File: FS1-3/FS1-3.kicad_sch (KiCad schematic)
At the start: 63 parts, among them U1 74LS54, U10 74LS51, U11 74HC02, U12 74AHC04, U13 74LS51, U14 74HC00, U15 74LS51, U16 74LS51, U17 74LS51, U18 74AHC04, U19 74LS51, U2 74LS51, U20 74LS51, U21 74LS51, U22 74AHC04, U23 74LS51, U24 74LS51, U25 74LS51, U26 74LS51, U27 74LS51, U28 74LS51, U29 74LS51, U3 74LS54, U30 74AHC04, U31 74LS51, U32 74LS54, U33 74LS54, U34 74LS54, U35 74LS54, U36 74LS51, U37 74LS51, U38 74LS51, U39 74LS51, U4 74LS51, U40 74AHC04, U41 74AHC04, U42 74HC02, U43 74HC00, U44 74LS51, U45 74LS51, U46 74LS51, U47 74LS51, U48 74AHC04, U49 74AHC04, U5 74LS54, U50 74AHC04, U51 74LS51, U52 74LS51, U53 74LS51, U54 74LS51, U55 74LS51, U56 74LS51, U57 74LS51, U58 74LS51, U59 74LS51, U6 74LS51, U60 74LS51, U61 74LS51, U62 74LS51, U7 74LS54, U8 74LS51, U9 74AHC04

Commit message: initial work on schematics for a backplane to which all boards will be attached.
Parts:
- renumbered U36 to 1A_P2, U32 to 1B_P2
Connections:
- net +NAND: now also U16.9, U21.9, U26.9, U31.9, U59.9, U60.9, U61.9, U62.9; no longer U16.4, U21.4, U26.4, U31.4, U59.4, U60.4, U61.4, U62.4
- net +P10: now also U37.1; no longer U37.2
- net +P11: now also 1A_P2.1; no longer 1A_P2.2
- net +P4: now also U2.1; no longer U2.2
- net +P5: now also U4.1; no longer U4.2
- net +P6: now also U6.1; no longer U6.2
- net +P7: now also U8.1; no longer U8.2
- net +P8: now also U39.1; no longer U39.2
- net +P9: now also U38.1; no longer U38.2
- net +RD0: now also U2.9; no longer U2.4
- net +RD1: now also U4.9; no longer U4.4
- net +RD2: now also U6.9; no longer U6.4
- net +RD3: now also U8.9; no longer U8.4
- net +RD4: now also U39.9; no longer U39.4
- net +RD5: now also U38.9; no longer U38.4
- net +RD6: now also U37.9; no longer U37.4
- net +RD7: now also 1A_P2.9; no longer 1A_P2.4
- net +SOXOR: now also U16.13, U21.13, U26.13, U31.13, U59.13, U60.13, U61.13, U62.13; no longer U16.3, U21.3, U26.3, U31.3, U59.3, U60.3, U61.3, U62.3
- net +VUR: now also U12.1, U28.9, U29.9, U41.1, U51.9, U52.9; no longer U12.3, U28.4, U29.4, U41.3, U51.4, U52.4
- net +Z0: now also U16.8; no longer U16.6
- net +Z1: now also U21.8; no longer U21.6
- net +Z2: now also U26.8; no longer U26.6
- net +Z3: now also U31.8; no longer U31.6
- net +Z4: now also U62.8; no longer U62.6
- net +Z5: now also U61.8; no longer U61.6
- net +Z6: now also U60.8; no longer U60.6
- net +Z7: now also U59.8; no longer U59.6
- net -C1: now also U12.1, U13.11, U15.1, U20.8; no longer U12.11, U13.5, U15.2, U20.6
- net -C5: now also U41.1, U55.8, U56.11, U58.1; no longer U41.11, U55.6, U56.5, U58.2
- net -X1: now also U11.2, U14.1, U17.9, U9.1; no longer U11.5, U14.4, U17.4, U9.5
- net -X2: now also U23.9, U25.9, U9.1; no longer U23.4, U25.4, U9.13
- net -X3: now also U11.2, U12.1, U14.1, U27.9; no longer U11.11, U12.13, U14.12, U27.4
- net -X4: now also U40.1, U42.2, U45.9, U58.9; no longer U40.11, U42.8, U45.4, U58.4
- net -X5: now also U40.1, U42.2, U43.1, U44.9; no longer U40.5, U42.5, U43.4, U44.4
- net -X6: now also U40.1, U47.9, U57.9; no longer U40.13, U47.4, U57.4
- net -X7: now also U41.1, U42.2, U43.1, U46.9; no longer U41.13, U42.11, U43.12, U46.4
- net -XOR: now also U14.1, U20.13, U28.13, U43.1, U52.13, U55.13; no longer U14.9, U20.3, U28.3, U43.9, U52.3, U55.3
- net -Y1: now also U11.3, U14.2, U17.11, U4.8, U9.1; no longer U11.6, U14.5, U17.5, U4.6, U9.3
- net -Y2: now also U23.11, U25.11, U6.8; no longer U23.5, U25.5, U6.6
- net -Y3: now also U11.3, U14.2, U27.11, U8.8; no longer U11.12, U14.13, U27.5, U8.6
- net -Y4: now also U39.8, U40.1, U42.3, U45.11, U58.11; no longer U39.6, U40.9, U42.9, U45.5, U58.5
- net -Y5: now also U38.8, U40.1, U42.3, U43.2, U44.11; no longer U38.6, U40.3, U42.6, U43.5, U44.5
- net -Y6: now also U37.8, U47.11, U57.11; no longer U37.6, U47.5, U57.5
- net -Y7: now also 1A_P2.8, U42.3, U43.2, U46.11; no longer 1A_P2.6, U42.12, U43.13, U46.5
- net AC/X: now also 1A_P2.10, U2.11, U37.11, U38.11, U39.11, U4.11, U6.11, U8.11; no longer 1A_P2.5, U2.5, U37.5, U38.5, U39.5, U4.5, U6.5, U8.5
- net C0: now also U15.8; no longer U15.6
- net C4: now also U58.8; no longer U58.6
- net P/Y: now also 1A_P2.13, U2.13, U37.13, U38.13, U39.13, U4.13, U6.13, U8.13; no longer 1A_P2.3, U2.3, U37.3, U38.3, U39.3, U4.3, U6.3, U8.3
- net X0: now also U10.9, U11.2, U15.9, U9.1; no longer U10.4, U11.8, U15.4, U9.11
- net Y0: now also U10.11, U11.3, U15.11, U2.8, U9.1; no longer U10.5, U11.9, U15.5, U2.6, U9.9
- net at U12.2: now also U27.1; no longer U27.2
- net at U43.3: now also U58.13; no longer U58.3
- net at U41.2: now also U46.1; no longer U46.2
- net at U14.3: now also U15.13; no longer U15.3
- net at U9.2: now also U23.1; no longer U23.2
- net at U40.2: now also U47.1; no longer U47.2
- new net: U41.1, U45.8, U56.9
- new net: U41.2, U56.1
- new net: U14.3, U28.11
- new net: U12.2, U27.13
- new net: U27.8, U29.1, U30.1
- new net: U40.2, U44.1
- new net: U40.2, U44.13
- new net: U44.8, U49.1, U54.1
- new net: U43.3, U52.11
- new net: U11.1, U20.1, U21.11
- new net: U14.3, U20.11
- new net: U18.1, U19.9, U20.9, U25.8
- new net: U11.1, U14.2, U16.11
- new net: U42.1, U43.2, U60.11
- new net: U43.3, U57.13
- new net: U17.8, U18.1, U19.1
- new net: U18.2, U19.11
- new net: U40.2, U45.1
- new net: U42.1, U52.1, U59.11
- new net: U48.1, U52.8, U53.11, U57.1
- new net: U54.8, U61.1
- new net: U42.1, U55.1, U61.11
- new net: U56.8, U62.1
- new net: U42.1, U43.2, U62.11
- new net: U41.2, U51.13
- new net: U49.1, U54.9, U55.9, U57.8
- new net: U17.13, U9.2
- new net: U11.1, U28.1, U31.11
- new net: U22.1, U24.11, U25.1, U28.8
- new net: U46.8, U50.1, U51.1
- new net: U50.2, U51.11
- new net: U43.3, U55.11
- new net: U13.8, U16.1
- new net: U22.2, U24.13
- new net: U49.2, U54.11
- new net: U49.2, U54.13
- new net: U14.3, U25.13
- new net: U19.8, U21.1
- new net: U53.8, U60.1
- new net: U41.2, U46.13
- new net: U40.2, U47.13
- new net: U29.11, U30.2
- new net: U12.2, U29.13
- new net: U29.8, U31.1
- new net: U48.2, U53.13
- new net: U40.2, U45.13
- new net: U18.2, U19.13
- new net: U11.1, U14.2, U26.11
- new net: U10.1, U9.2
- new net: U10.13, U9.2
- new net: U10.8, U12.1, U13.9
- new net: U47.8, U48.1, U53.9
- new net: U48.2, U53.1
- new net: U12.2, U13.1
- new net: U12.2, U13.13
- new net: U51.8, U59.1
- new net: U41.2, U56.13
- new net: U23.13, U9.2
- new net: U22.1, U23.8, U24.9
- new net: U22.2, U24.1
- new net: U24.8, U26.1
- new net: U17.1, U9.2
- no-connect marks 0 -> 2

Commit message: first review and many fixes to FS1-3 board
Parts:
- removed U1, U3, U5, U7: 74LS54, symbol 74xx:74LS54
- removed U10, U13, U15, U16, U17, U19, U2, U20, U21, U23, U24, U25, U26, U27, U28, U29, U31, U4, U6, U8: 74LS51, symbol 74xx:74LS51
- removed U11 (x4): 74HC02, symbol 74xx:74HC02
- removed U12 (x5), U18 (x2), U22 (x2), U30, U9 (x6): 74AHC04, symbol 74xx:74AHC04
- removed U14 (x4): 74HC00, symbol 74xx:74HC00
- gave numbers to parts that had none: 1
- renumbered U37 to 1A_P2A_, 1A_P2 to 1A_P2A_, 1B_P2 to 1B_P2A_, U40 to 1C_P2A_, U41 to 1C_P2A_, U48 to 1C_P2A_, U46 to 1D_P2A_, U47 to 1D_P2A_, U52 to 1E_P2A_, U51 to 1E_P2A_, U60 to 1F_P2A_, U59 to 1F_P2A_, U42 to 2C_P2A_, U39 to 3A_P2A_, U38 to 3A_P2A_, U33 to 3B_P2A_, U42 to 3C_P2A_, U57 to 3D_P2A_, U53 to 3D_P2A_, U49 to 3E_P2A_, U48 to 3E_P2A_, U41 to 3E_P2A_, U61 to 3F_P2A_, U62 to 3F_P2A_, U43 to 4C_P2A_, U34 to 5A_P2A_, U35 to 5B_P2A_, U41 to 5C_P2A_, U40 to 5C_P2A_, U44 to 5D_P2A_, U45 to 5D_P2A_, U55 to 5E_P2A_, U54 to 5E_P2A_, U58 to 5F_P2A_, U56 to 5F_P2A_
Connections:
- net +AC4: now also CONECTOR_P2A.62 (P62)
- net +AC5: now also 5A_P2A_.13, CONECTOR_P2A.66 (P66); no longer 5A_P2A_.1
- net +AC6: now also CONECTOR_P2A.15 (P15)
- net +AC7: now also CONECTOR_P2A.38 (P38)
- net +CI10: now also 3B_P2A_.5, CONECTOR_P2A.16 (P16); no longer 3B_P2A_.4
- net +CI11: now also 1B_P2A_.5, CONECTOR_P2A.39 (P39); no longer 1B_P2A_.4
- net +CI8: now also CONECTOR_P2A.63 (P63)
- net +CI9: now also 5A_P2A_.5, CONECTOR_P2A.64 (P64); no longer 5A_P2A_.4
- net +NAND: now also 1F_P2A_.1, 1F_P2A_.2, 3F_P2A_.4, CONECTOR_P2A.60 (P60); no longer 1F_P2A_.9, 1F_P2A_.9, 3F_P2A_.9
- net +P10: now also 1A_P2A_.2, CONECTOR_P2A.40 (P40); no longer 1A_P2A_.1
- net +P11: now also CONECTOR_P2A.4 (P4)
- net +P8: now also CONECTOR_P2A.52 (P52)
- net +P9: now also 3A_P2A_.3, CONECTOR_P2A.17 (P17); no longer 3A_P2A_.1
- net +RD4: now also CONECTOR_P2A.55 (P55)
- net +RD5: now also 3A_P2A_.4, CONECTOR_P2A.53 (P53); no longer 3A_P2A_.9
- net +RD6: now also 1A_P2A_.4, CONECTOR_P2A.41 (P41); no longer 1A_P2A_.9
- net +RD7: now also CONECTOR_P2A.42 (P42)
- net +RE10: now also CONECTOR_P2A.20 (P20)
- net +RE11: now also CONECTOR_P2A.43 (P43)
- net +RE8: now also 5B_P2A_.10, CONECTOR_P2A.67 (P67); no longer 5B_P2A_.9
- net +RE9: now also CONECTOR_P2A.31 (P31)
- net +SOXOR: now also 1F_P2A_.10, 1F_P2A_.4, 3F_P2A_.1, 3F_P2A_.2, CONECTOR_P2A.34 (P34); no longer 1F_P2A_.13, 1F_P2A_.13, 3F_P2A_.13, 3F_P2A_.13
- net +VUR: now also 1E_P2A_.1, 1E_P2A_.4, CONECTOR_P2A.2 (P2), U41.3; no longer 1E_P2A_.9, 1E_P2A_.9, U41.1
- net +Z4: now also 3F_P2A_.6, CONECTOR_P2A.56 (P56); no longer 3F_P2A_.8
- net +Z5: now also CONECTOR_P2A.58 (P58)
- net +Z6: now also CONECTOR_P2A.47 (P47)
- net +Z7: now also 1F_P2A_.6, CONECTOR_P2A.37 (P37); no longer 1F_P2A_.8
- net -AC4: now also 5B_P2A_.3, CONECTOR_P2A.28 (P28); no longer 5B_P2A_.2
- net -AC5: now also 5A_P2A_.3, CONECTOR_P2A.30 (P30); no longer 5A_P2A_.2
- net -AC6: now also 3B_P2A_.3, CONECTOR_P2A.51 (P51); no longer 3B_P2A_.2
- net -AC7: now also 1B_P2A_.3, CONECTOR_P2A.3 (P3); no longer 1B_P2A_.2
- net -AC/X: now also 1B_P2A_.2, 3B_P2A_.2, 5A_P2A_.2, 5B_P2A_.2, CONECTOR_P2A.65 (P65); no longer 1B_P2A_.3, 3B_P2A_.3, 5A_P2A_.3, 5B_P2A_.3
- net -C5: now also 3E_P2A_.9, 5F_P2A_.4, 5F_P2A_.9, CONECTOR_P2A.68 (P68); no longer 3E_P2A_.1, 5F_P2A_.1, 5F_P2A_.11
- net -X4: now also 3C_P2A_.9, 5C_P2A_.11, 5D_P2A_.1, 5F_P2A_.3; no longer 3C_P2A_.2, 5C_P2A_.1, 5D_P2A_.9, 5F_P2A_.9
- net -X5: now also 3C_P2A_.5, 4C_P2A_.4, 5C_P2A_.5, 5D_P2A_.4; no longer 3C_P2A_.2, 4C_P2A_.1, 5C_P2A_.1, 5D_P2A_.9
- net -X6: now also 1C_P2A_.13, 1D_P2A_.4, 2C_P2A_.12, 3D_P2A_.10; no longer 1C_P2A_.1, 1D_P2A_.9, 2C_P2A_.2, 3D_P2A_.9
- net -X7: now also 1D_P2A_.13; no longer 1D_P2A_.9
- net -XOR: now also 1E_P2A_.9, 4C_P2A_.10, 4C_P2A_.12, CONECTOR_P2A.61 (P61); no longer 1E_P2A_.13, 4C_P2A_.1, 4C_P2A_.1
- net -Y4: now also 3C_P2A_.8, 5C_P2A_.9, 5D_P2A_.13, 5F_P2A_.2; no longer 3C_P2A_.3, 5C_P2A_.1, 5D_P2A_.11, 5F_P2A_.11
- net -Y5: now also 3A_P2A_.6, 3C_P2A_.6, 4C_P2A_.5, 5C_P2A_.3, 5D_P2A_.5; no longer 3A_P2A_.8, 3C_P2A_.3, 4C_P2A_.2, 5C_P2A_.1, 5D_P2A_.11
- net -Y6: now also 1A_P2A_.6, 1C_P2A_.5, 1D_P2A_.5, 2C_P2A_.11, 3D_P2A_.9; no longer 1A_P2A_.8, 1C_P2A_.1, 1D_P2A_.11, 2C_P2A_.3, 3D_P2A_.11
- net -Y7: now also 1C_P2A_.3, 1D_P2A_.1; no longer 1C_P2A_.1, 1D_P2A_.11
- net AC/X: now also 5A_P2A_.1, CONECTOR_P2A.33 (P33); no longer 1A_P2A_.10, 1A_P2A_.11, 3A_P2A_.11, 3A_P2A_.11, 5A_P2A_.13
- net C1/X: now also 1B_P2A_.4, 3B_P2A_.4, 5A_P2A_.4; no longer 1B_P2A_.5, 3B_P2A_.5, 5A_P2A_.5
- net C4: now also 5F_P2A_.6; no longer 5F_P2A_.8
- net P/Y: now also 1A_P2A_.3, 3A_P2A_.2, CONECTOR_P2A.5 (P5); no longer 1A_P2A_.13, 3A_P2A_.13
- net RE/X: now also 5B_P2A_.9, CONECTOR_P2A.32 (P32); no longer 5B_P2A_.10
- net at 5F_P2A_.1: now also 5C_P2A_.12; no longer 5C_P2A_.2
- net at 4C_P2A_.3: now also 1E_P2A_.13; no longer 1E_P2A_.11
- net at 3D_P2A_.13: now also 4C_P2A_.11; no longer 4C_P2A_.3
- net at 1E_P2A_.10: now also 1F_P2A_.3, 3C_P2A_.1
- net at 1E_P2A_.8, 3D_P2A_.1: now also 3D_P2A_.4, 3E_P2A_.5; no longer 3D_P2A_.11, 3E_P2A_.1
- net at 3F_P2A_.10: now also 3C_P2A_.4, 5E_P2A_.1
- net RD/Y: now reaches 3A_P2A_.10
- net RD/Y: now also 1A_P2A_.10, 1A_P2A_.5, 3A_P2A_.5, CONECTOR_P2A.7 (P7)
- net at 5F_P2A_.8: now also 3F_P2A_.3; no longer 3F_P2A_.1
- net at 5E_P2A_.10: now also 3D_P2A_.8, 3E_P2A_.11, 5E_P2A_.5
- net at 5E_P2A_.11: no longer 4C_P2A_.3
- net at 1D_P2A_.10: now also 1C_P2A_.2
- net at 5D_P2A_.10: now also 5C_P2A_.8
- net at 5F_P2A_.13: now also 3E_P2A_.8; no longer 3E_P2A_.2
- net at 5F_P2A_.10: now also 5C_P2A_.13, 5D_P2A_.8
- removed net ?: CONECTOR_P2A.1 (P1), CONECTOR_P2A.10 (P10), CONECTOR_P2A.11 (P11), CONECTOR_P2A.12 (P12), CONECTOR_P2A.13 (P13), CONECTOR_P2A.14 (P14), CONECTOR_P2A.15 (P15), CONECTOR_P2A.16 (P16), CONECTOR_P2A.17 (P17), CONECTOR_P2A.18 (P18), CONECTOR_P2A.19 (P19), CONECTOR_P2A.2 (P2), CONECTOR_P2A.20 (P20), CONECTOR_P2A.21 (P21), CONECTOR_P2A.22 (P22), CONECTOR_P2A.23 (P23), CONECTOR_P2A.24 (P24), CONECTOR_P2A.25, CONECTOR_P2A.26 (P26), CONECTOR_P2A.27 (P27), CONECTOR_P2A.28 (P28), CONECTOR_P2A.29 (P29), CONECTOR_P2A.3 (P3), CONECTOR_P2A.30 (P30), CONECTOR_P2A.31 (P31), CONECTOR_P2A.32 (P32), CONECTOR_P2A.33 (P33), CONECTOR_P2A.34 (P34), CONECTOR_P2A.35 (P35), CONECTOR_P2A.36 (P36), CONECTOR_P2A.37 (P37), CONECTOR_P2A.38 (P38), CONECTOR_P2A.39 (P39), CONECTOR_P2A.4 (P4), CONECTOR_P2A.40 (P40), CONECTOR_P2A.41 (P41), CONECTOR_P2A.42 (P42), CONECTOR_P2A.43 (P43), CONECTOR_P2A.44 (P44), CONECTOR_P2A.45 (P45), CONECTOR_P2A.46 (P46), CONECTOR_P2A.47 (P47), CONECTOR_P2A.48 (P48), CONECTOR_P2A.49 (P49), CONECTOR_P2A.5 (P5), CONECTOR_P2A.50 (P50), CONECTOR_P2A.51 (P51), CONECTOR_P2A.52 (P52), CONECTOR_P2A.53 (P53), CONECTOR_P2A.54 (P54), CONECTOR_P2A.55 (P55), CONECTOR_P2A.56 (P56), CONECTOR_P2A.57 (P57), CONECTOR_P2A.58 (P58), CONECTOR_P2A.59 (P59), CONECTOR_P2A.6 (P6), CONECTOR_P2A.60 (P60), CONECTOR_P2A.61 (P61), CONECTOR_P2A.62 (P62), CONECTOR_P2A.63 (P63), CONECTOR_P2A.64 (P64), CONECTOR_P2A.65 (P65), CONECTOR_P2A.66 (P66), CONECTOR_P2A.67 (P67), CONECTOR_P2A.68 (P68), CONECTOR_P2A.69 (P69), CONECTOR_P2A.7 (P7), CONECTOR_P2A.70 (P70), CONECTOR_P2A.8 (P8), CONECTOR_P2A.9 (P9)
- new net: 5C_P2A_.6, 5D_P2A_.2
- new net: 5C_P2A_.4, 5D_P2A_.3
- new net: 3E_P2A_.13, 5D_P2A_.6, 5E_P2A_.2
- new net: 1F_P2A_.13, 2C_P2A_.13, 4C_P2A_.13
- new net: 3F_P2A_.13, 5E_P2A_.6
- new net: 3C_P2A_.10, 3F_P2A_.5, 4C_P2A_.9
- new net: 1E_P2A_.3, U41.4
- new net: 1E_P2A_.5, U50.10
- new net: 1D_P2A_.8, 1E_P2A_.2, U50.11
- new net: 4C_P2A_.6, 5E_P2A_.9
- new net: 3E_P2A_.10, 5E_P2A_.3
- new net: 3E_P2A_.12, 5E_P2A_.4
- new net: 1F_P2A_.9, 3D_P2A_.6
- new net: 4C_P2A_.8, 5F_P2A_.5
- new net: 1C_P2A_.4, 1D_P2A_.9
- new net: 1C_P2A_.12, 1D_P2A_.2
- new net: 3D_P2A_.3, 3E_P2A_.6
- new net: 5C_P2A_.10, 5D_P2A_.9
- new net: 1C_P2A_.8, 3D_P2A_.2
- new net: 1C_P2A_.9, 1D_P2A_.6, 3D_P2A_.5
- new net: 1E_P2A_.6, 1F_P2A_.5
- new net: 1C_P2A_.6, 1D_P2A_.3
- new net +C4: CONECTOR_P2A.57 (P57)
- new net CI/X: CONECTOR_P2A.29 (P29)
- new net GND: CONECTOR_P2A.70 (P70)
- new net VCC: CONECTOR_P2A.1 (P1)
- now unconnected: 1F_P2A_.11, 3F_P2A_.11
- no-connect marks 2 -> 48
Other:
- moved on the sheet: 1C_P2A_A, 1C_P2A_D, 1C_P2A_F, 1D_P2A_A, 1E_P2A_A, 1F_P2A_A, 3A_P2A_A, 3C_P2A_C, 3E_P2A_D, 3E_P2A_F, 4C_P2A_C, 5B_P2A_A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

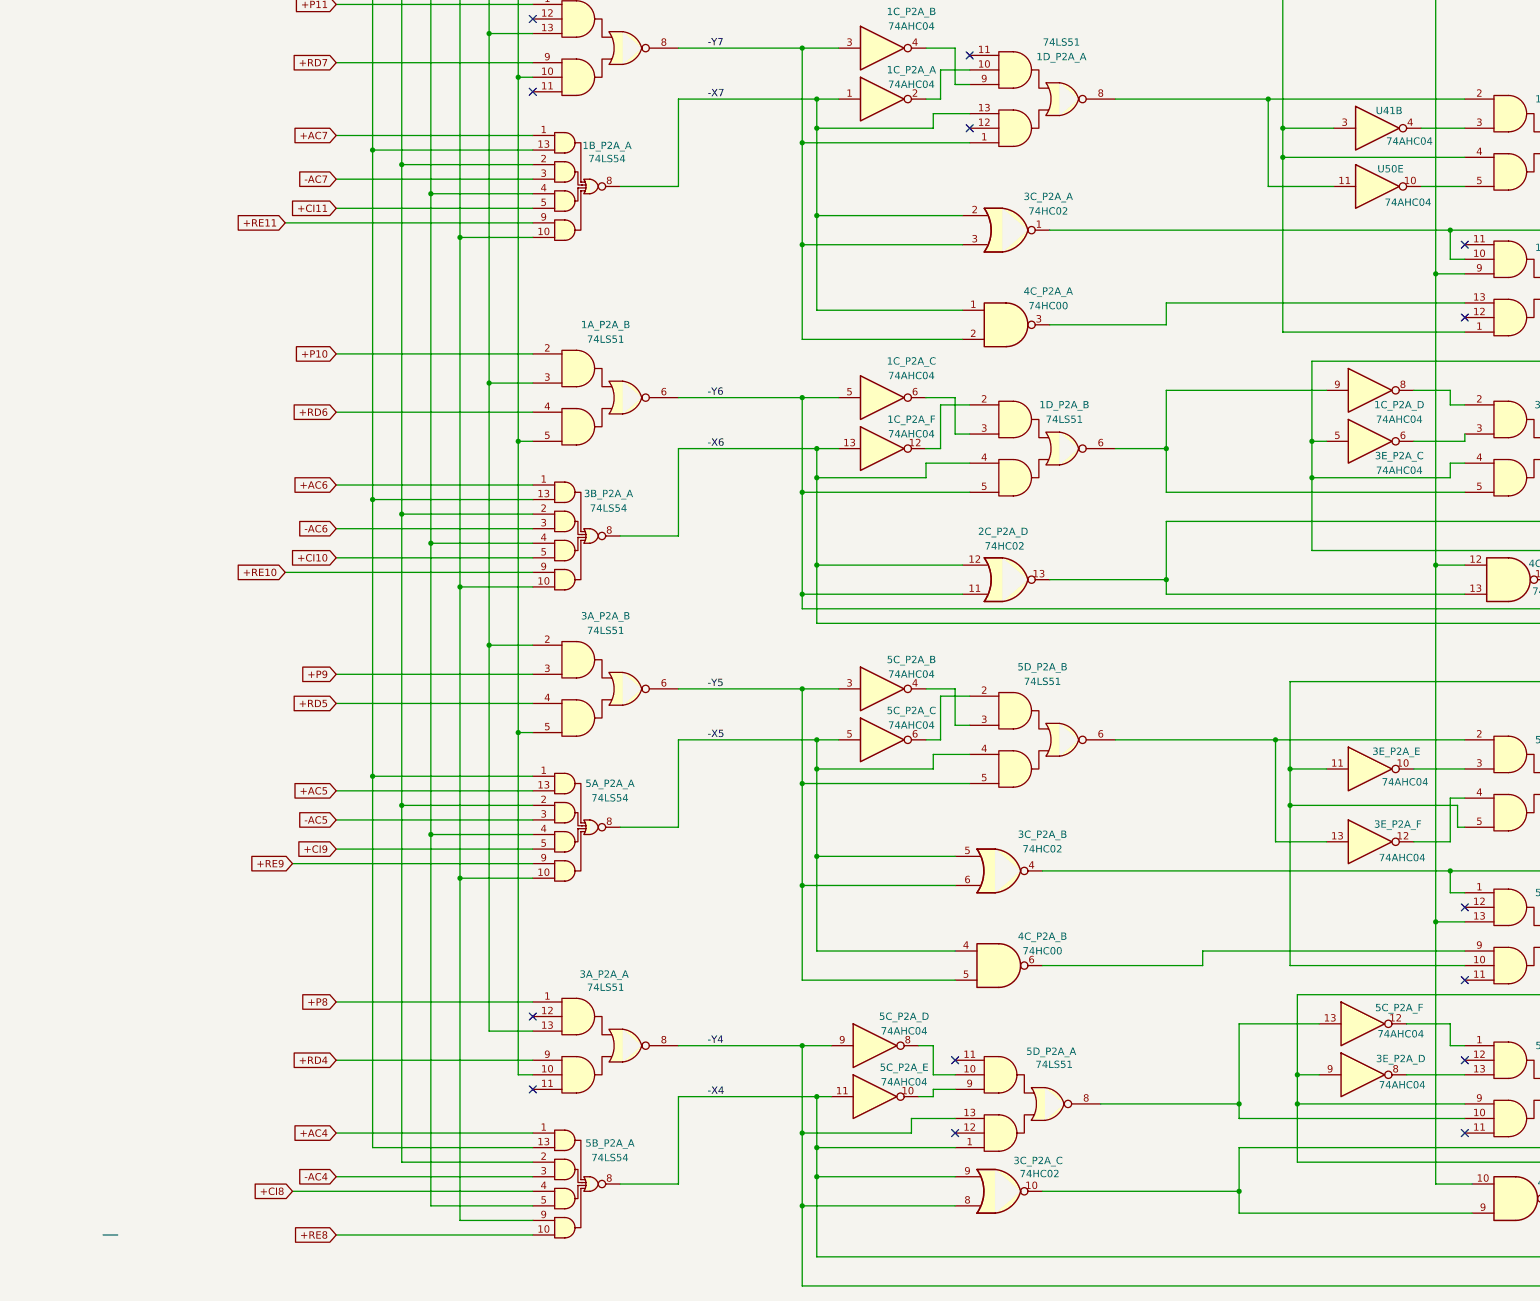
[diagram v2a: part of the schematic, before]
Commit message: adding references to a couple NOT gates that are not annotated in the original schematics.
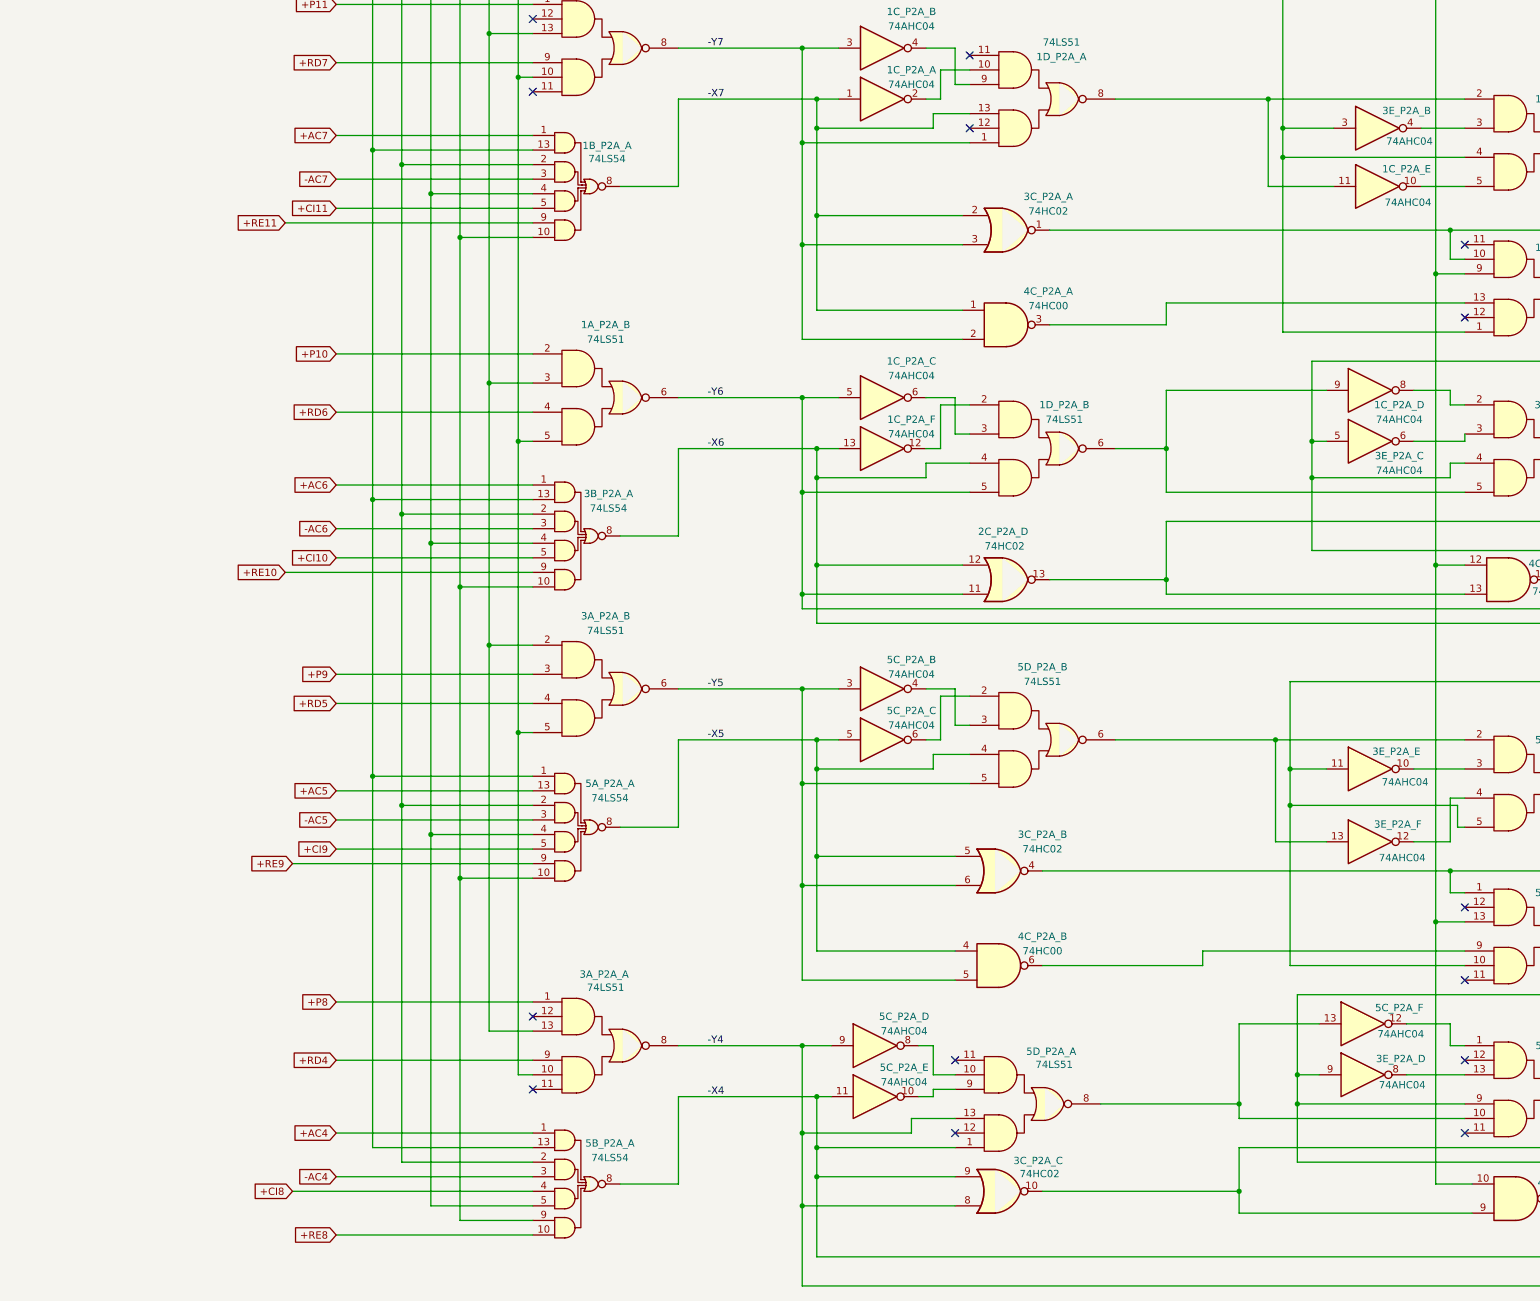
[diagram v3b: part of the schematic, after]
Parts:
- renumbered U50 to 1C_P2A_, U41 to 3E_P2A_
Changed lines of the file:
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@@
 		)
 	)
-	(polyline
-		(pts
-			(xy 219.71 308.61) (xy 217.17 308.61)
-		)
-		(stroke
-			(width 0)
-			(type default)
-		)
-	)
 	(wire
 		(pts
@@
 		(in_pos_files yes)
 		(dnp no)
-		(property "Reference" "U?"
-			(at 441.452 112.522 0)
+		(property "Reference" "3E_P2A_"
+			(at 444.5 112.522 0)
 			(show_name no)
 			(do_not_autoplace no)
@@
 			(project "patinhofeio"
 				(path "/aca06203-542d-4682-a7e3-8839e24cce95/513c6191-fb8d-4702-a239-0db81c50d326"
-					(reference "U?")
+					(reference "3E_P2A_")
 					(unit 2)
 				)
@@
 		(in_pos_files yes)
 		(dnp no)
-		(property "Reference" "U?"
-			(at 441.706 122.682 0)
+		(property "Reference" "1C_P2A_"
+			(at 444.5 122.682 0)
 			(show_name no)
 			(do_not_autoplace no)
@@
 			(project "patinhofeio"
 				(path "/aca06203-542d-4682-a7e3-8839e24cce95/513c6191-fb8d-4702-a239-0db81c50d326"
-					(reference "U?")
+					(reference "1C_P2A_")
 					(unit 5)
 				)
